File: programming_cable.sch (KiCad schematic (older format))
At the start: 11 parts, among them J1 Conn_02x03_Male

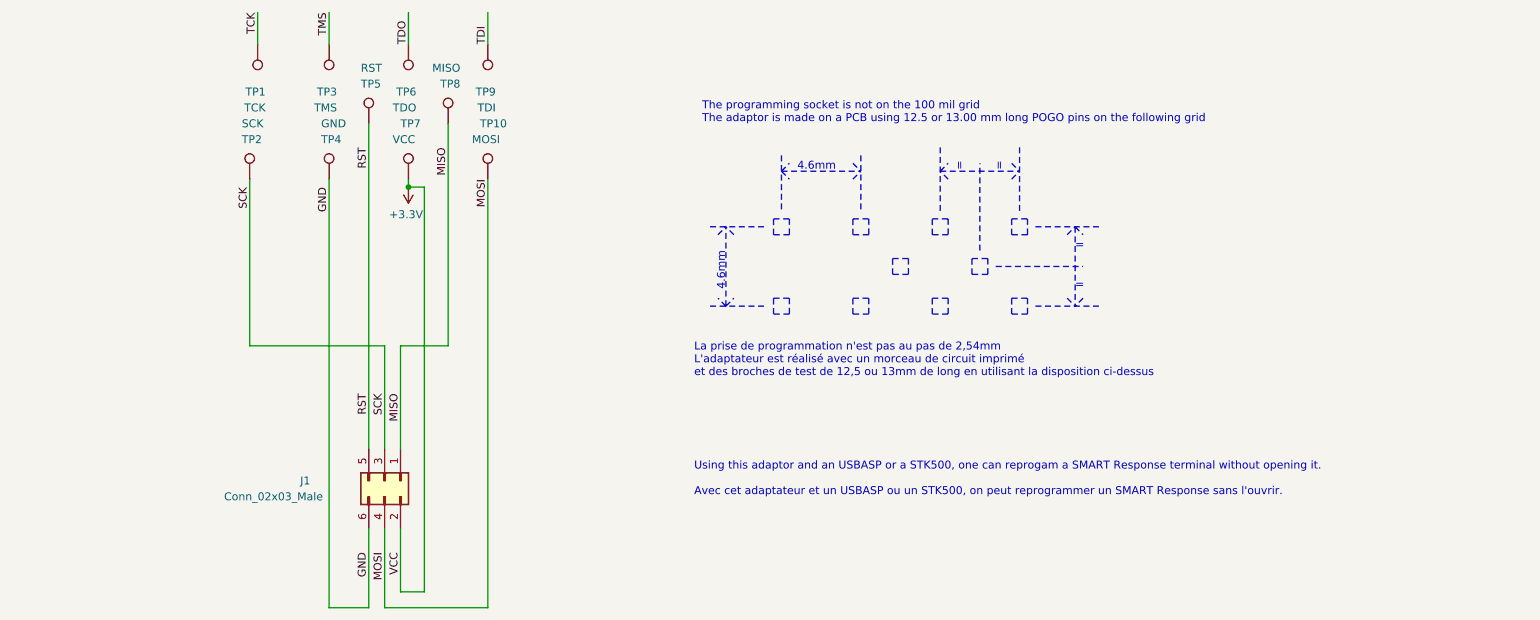
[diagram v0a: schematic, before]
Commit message: Updated schematics
Added some comment
Updated reference of U1 in Smart_Response_XE.sch (and .pdf too)
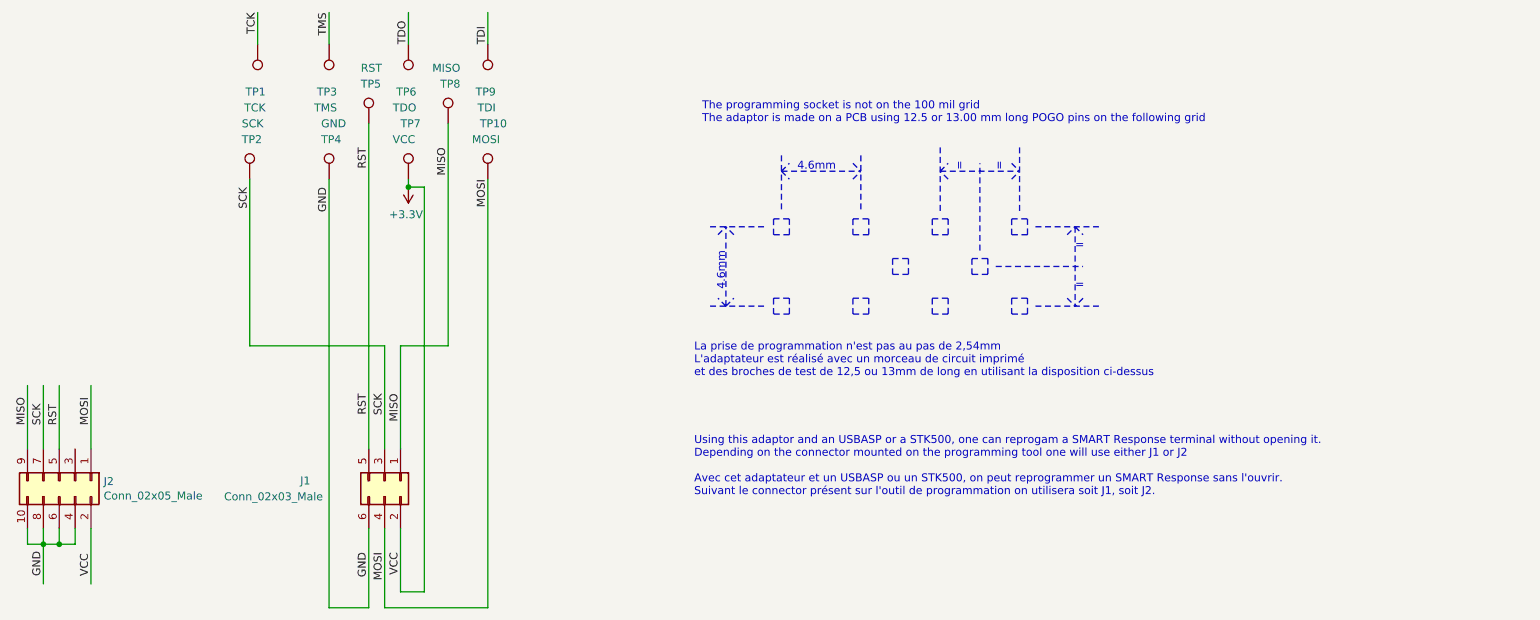
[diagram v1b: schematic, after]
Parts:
- added J2: Conn_02x05_Male, symbol Connector_Generic:Conn_02x05_Odd_Even
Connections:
- wire segments 22 -> 35
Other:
- note added: "Using this adaptor and an USBASP or a STK500, one can reprogam a SMART Response terminal without opening it.\nDepending on the connector mounted on the programming tool one will use either J1 or J2\n\nAvec cet adaptateur et un USBASP ou un STK500, on peut reprogrammer un SMART Response sans l'ouvrir.\nSuivant le connector présent sur l'outil de programmation on utilisera soit J1, soit J2."
- note removed: "Using this adaptor and an USBASP or a STK500, one can reprogam a SMART Response terminal without opening it.\n\nAvec cet adaptateur et un USBASP ou un STK500, on peut reprogrammer un SMART Response sans l'ouvrir."
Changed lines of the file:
@@
 Text Label 3450 4050 3    50   ~ 0
 RST
-Text Label 3650 5050 3    50   ~ 0
-VCC
-Text Label 3550 5050 3    50   ~ 0
-MOSI
-Text Label 3450 5050 3    50   ~ 0
-GND
 Wire Notes Line
 	6000 2950 6100 2950
@@
 	3200 2700 3200 5400
 Text Notes 5500 4700 0    50   ~ 0
-Using this adaptor and an USBASP or a STK500, one can reprogam a SMART Response terminal without opening it.\n\nAvec cet adaptateur et un USBASP ou un STK500, on peut reprogrammer un SMART Response sans l'ouvrir.
+Using this adaptor and an USBASP or a STK500, one can reprogam a SMART Response terminal without opening it.\nDepending on the connector mounted on the programming tool one will use either J1 or J2\n\nAvec cet adaptateur et un USBASP ou un STK500, on peut reprogrammer un SMART Response sans l'ouvrir.\nSuivant le connector présent sur l'outil de programmation on utilisera soit J1, soit J2.
 Wire Wire Line
 	3450 2350 3450 4400
@@
 Text Notes 7450 2650 1    50   ~ 0
 =
+$Comp
+L Connector_Generic:Conn_02x05_Odd_Even J2
+U 1 1 5E4A7CFA
+P 1500 4600
+F 0 "J2" V 1504 4880 50  0000 L CNN
+F 1 "Conn_02x05_Male" V 1595 4880 50  0000 L CNN
+F 2 "" H 1500 4600 50  0001 C CNN
+F 3 "~" H 1500 4600 50  0001 C CNN
+	1    1500 4600
+	0    1    1    0
+$EndComp
+Wire Wire Line
+	1700 4400 1700 4000
+Wire Wire Line
+	1500 4400 1500 4000
+Wire Wire Line
+	1400 4400 1400 4000
+Wire Wire Line
+	1300 4400 1300 4000
+Wire Wire Line
+	1700 4900 1700 5250
+Wire Wire Line
+	1600 4900 1600 5000
+Wire Wire Line
+	1600 5000 1500 5000
+Wire Wire Line
+	1500 4900 1500 5000
+Wire Wire Line
+	1500 5000 1400 5000
+Wire Wire Line
+	1400 5000 1400 4900
+Connection ~ 1500 5000
+Wire Wire Line
+	1400 5000 1300 5000
+Wire Wire Line
+	1300 5000 1300 4900
+Connection ~ 1400 5000
+Wire Wire Line
+	1400 5000 1400 5250
+Text Label 1700 4250 1    50   ~ 0
+MOSI
+Text Label 1500 4250 1    50   ~ 0
+RST
+Text Label 1400 4250 1    50   ~ 0
+SCK
+Text Label 1300 4250 1    50   ~ 0
+MISO
+Text Label 1700 5200 1    50   ~ 0
+VCC
+Text Label 1400 5200 1    50   ~ 0
+GND
+Text Label 3450 5050 3    50   ~ 0
+GND
+Text Label 3550 5050 3    50   ~ 0
+MOSI
+Text Label 3650 5050 3    50   ~ 0
+VCC
 $EndSCHEMATC
